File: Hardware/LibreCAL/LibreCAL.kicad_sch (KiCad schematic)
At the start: 4 parts

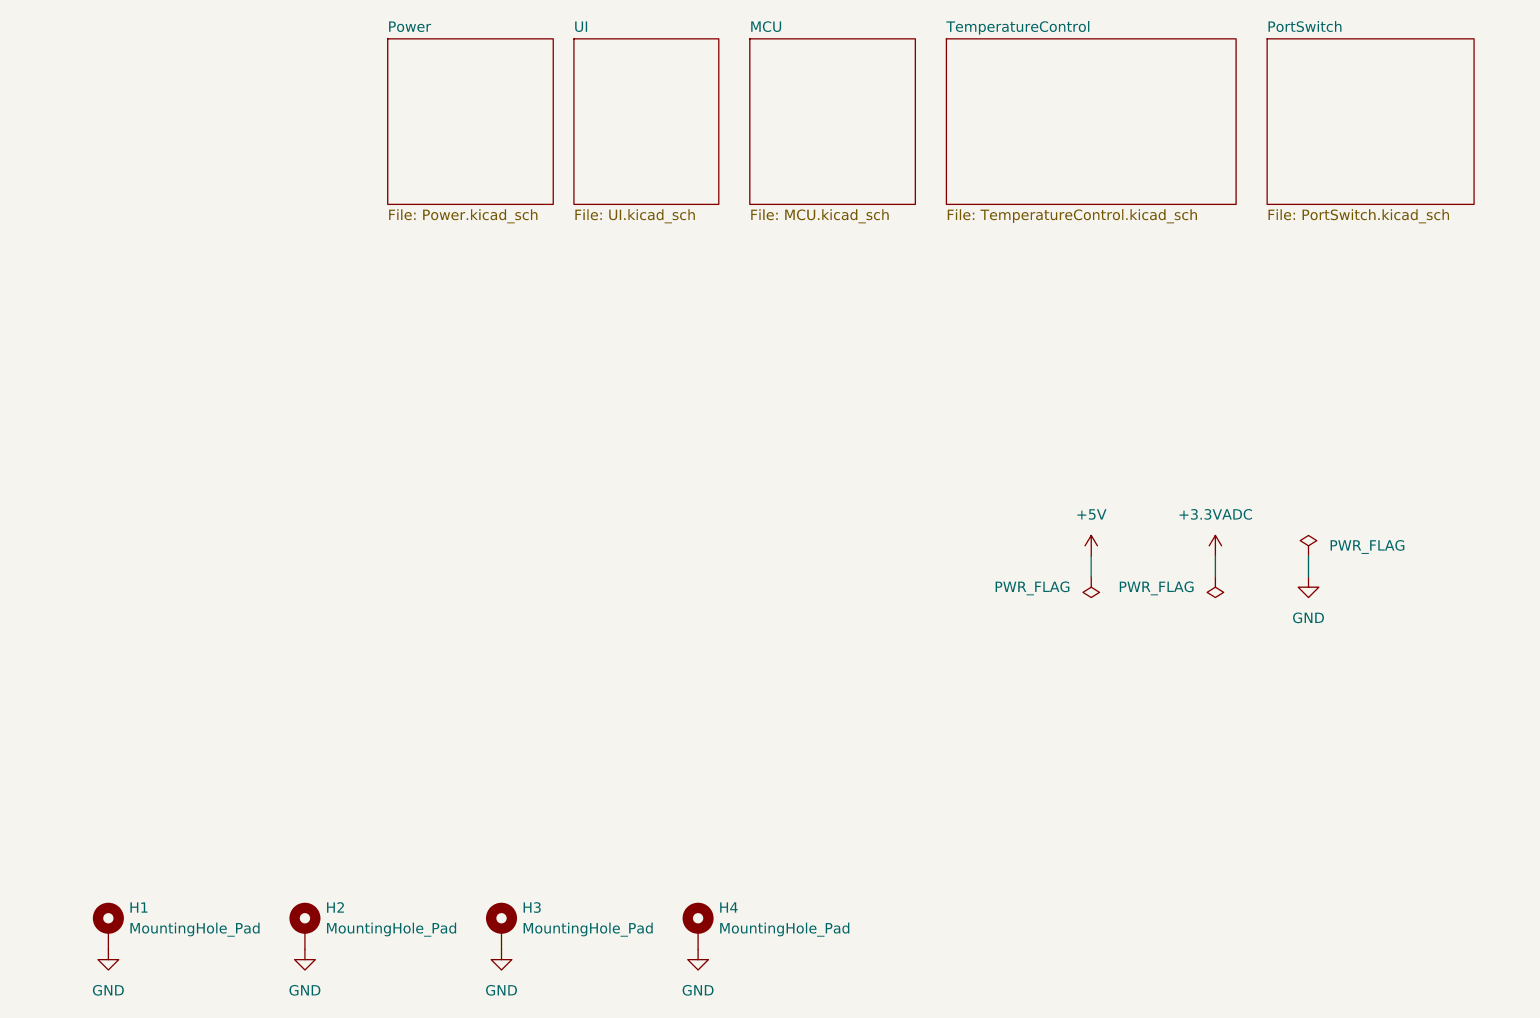
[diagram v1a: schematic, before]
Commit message: Filters added, housing updated
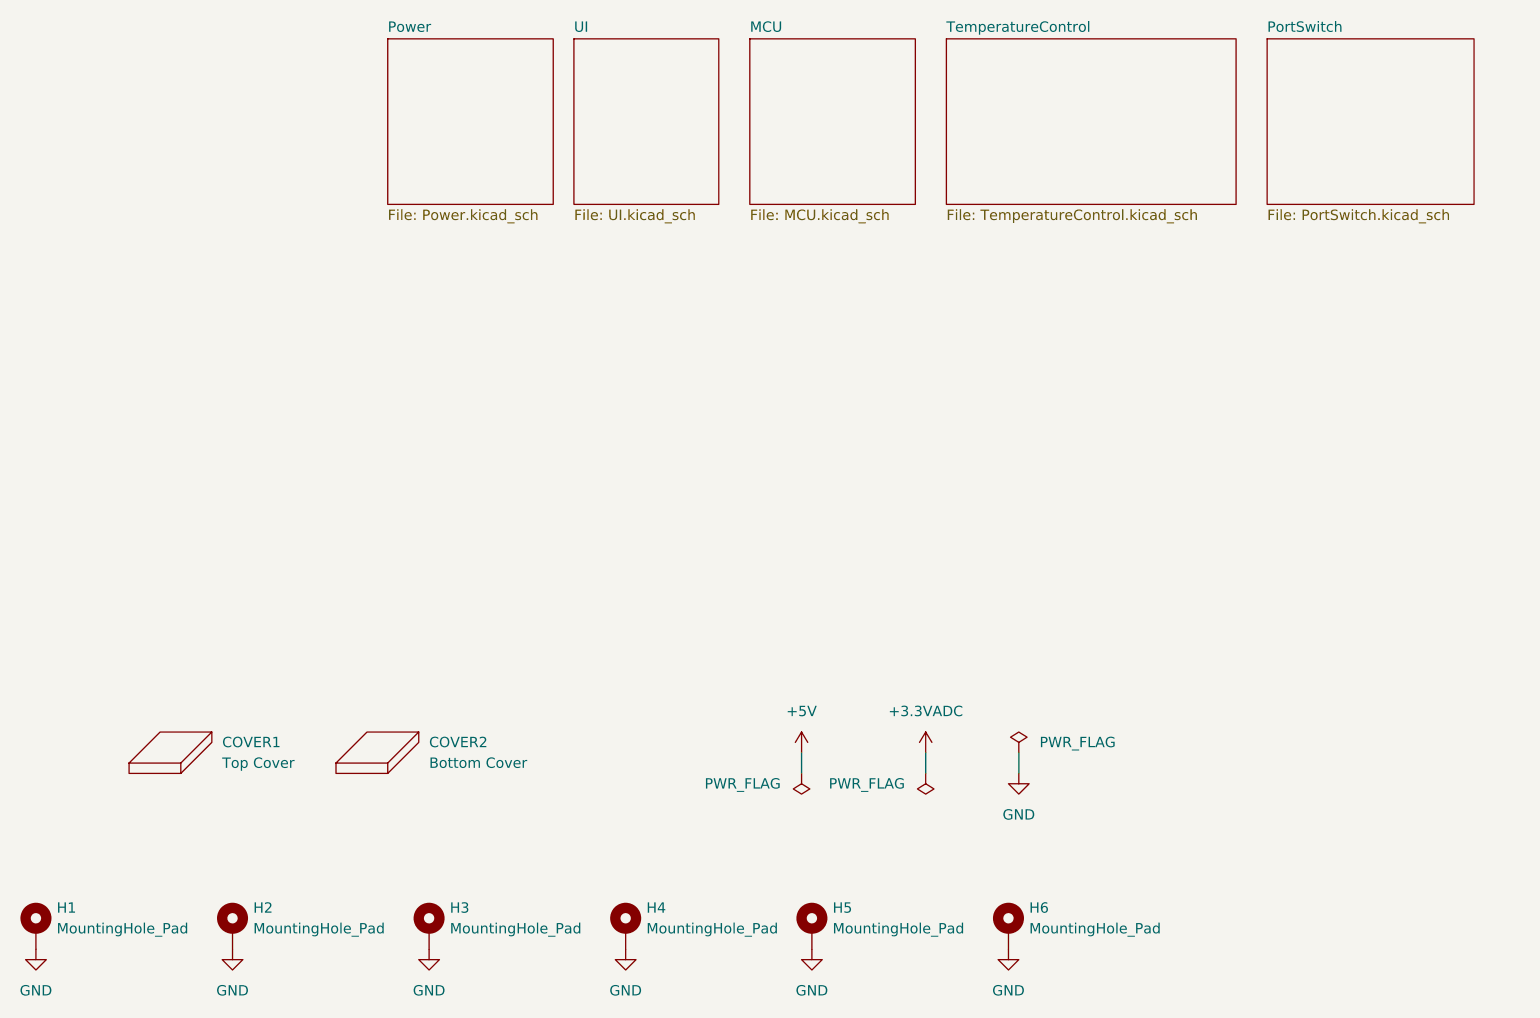
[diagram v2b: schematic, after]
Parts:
- added COVER1: Top Cover, LibreCAL:TopCover, symbol LibreCAL:Cover
- added COVER2: Bottom Cover, LibreCAL:BottomCover, symbol LibreCAL:Cover
- added H5, H6: MountingHole_Pad, MountingHole:MountingHole_3.2mm_M3_ISO14580_Pad_TopBottom, symbol Mechanical:MountingHole_Pad
- H1, H2, H3, H4: now left out of the parts list
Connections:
- net GND: now also H5.1, H6.1
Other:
- moved on the sheet: H1, H2, H3, H4

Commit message: Production files
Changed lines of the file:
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@@
     (pin "1")
+  )
+  (symbol (lib_id "LibreCAL:Cover") (at 72.39 154.94 0) (unit 1)
+    (in_bom no) (on_board yes) (fields_autoplaced)
+    (property "Reference" "COVER2" (id 0) (at 78.74 152.3999 0)
+      (effects (font (size 1.27 1.27)) (justify left))
+    )
+    (property "Value" "Bottom Cover" (id 1) (at 78.74 154.9399 0)
+      (effects (font (size 1.27 1.27)) (justify left))
+    )
+    (property "Footprint" "LibreCAL:BottomCover" (id 2) (at 72.39 154.94 0)
+      (effects (font (size 1.27 1.27)) hide)
+    )
+    (property "Datasheet" "" (id 3) (at 72.39 154.94 0)
+      (effects (font (size 1.27 1.27)) hide)
+    )
   )
   (symbol (lib_id "Mechanical:MountingHole_Pad") (at 149.86 176.53 0) (unit 1)
@@
     (pin "1")
   )
-  (symbol (lib_id "LibreCAL:Cover") (at 72.39 156.21 0) (unit 1)
+  (symbol (lib_id "LibreCAL:Cover") (at 46.99 154.94 0) (unit 1)
     (in_bom no) (on_board yes) (fields_autoplaced)
-    (property "Reference" "COVER2" (id 0) (at 78.74 153.6699 0)
-      (effects (font (size 1.27 1.27)) (justify left))
-    )
-    (property "Value" "Bottom Cover" (id 1) (at 78.74 156.2099 0)
-      (effects (font (size 1.27 1.27)) (justify left))
-    )
-    (property "Footprint" "LibreCAL:BottomCover" (id 2) (at 72.39 156.21 0)
-      (effects (font (size 1.27 1.27)) hide)
-    )
-    (property "Datasheet" "" (id 3) (at 72.39 156.21 0)
+    (property "Reference" "COVER1" (id 0) (at 53.34 152.3999 0)
+      (effects (font (size 1.27 1.27)) (justify left))
+    )
+    (property "Value" "Top Cover" (id 1) (at 53.34 154.9399 0)
+      (effects (font (size 1.27 1.27)) (justify left))
+    )
+    (property "Footprint" "LibreCAL:TopCover" (id 2) (at 46.99 154.94 0)
+      (effects (font (size 1.27 1.27)) hide)
+    )
+    (property "Datasheet" "" (id 3) (at 46.99 154.94 0)
       (effects (font (size 1.27 1.27)) hide)
     )
@@
     )
     (pin "1")
-  )
-  (symbol (lib_id "LibreCAL:Cover") (at 46.99 156.21 0) (unit 1)
-    (in_bom no) (on_board yes) (fields_autoplaced)
-    (property "Reference" "COVER1" (id 0) (at 53.34 153.6699 0)
-      (effects (font (size 1.27 1.27)) (justify left))
-    )
-    (property "Value" "Top Cover" (id 1) (at 53.34 156.2099 0)
-      (effects (font (size 1.27 1.27)) (justify left))
-    )
-    (property "Footprint" "LibreCAL:TopCover" (id 2) (at 46.99 156.21 0)
-      (effects (font (size 1.27 1.27)) hide)
-    )
-    (property "Datasheet" "" (id 3) (at 46.99 156.21 0)
-      (effects (font (size 1.27 1.27)) hide)
-    )
   )
   (symbol (lib_id "power:GND") (at 151.13 157.48 0) (unit 1)
@@
       (reference "C50") (unit 1) (value "NFM18CC223R1C3D") (footprint "LibreCAL:NFM18CC")
     )
-    (path "/dcda2e3f-39cb-4b5d-a0f7-3f67f2dd2c02"
+    (path "/a5774e18-31e1-4bb5-a8f4-b8516b668c1a"
       (reference "COVER1") (unit 1) (value "Top Cover") (footprint "LibreCAL:TopCover")
     )
-    (path "/ac162879-7480-449d-8f17-09ac1fe716ba"
+    (path "/3789b0ae-08e6-4dfa-af0f-48751ba38e44"
       (reference "COVER2") (unit 1) (value "Bottom Cover") (footprint "LibreCAL:BottomCover")
     )

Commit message: Improvements on LibreCAL KiCad: fixed minor errors/labels(cosmetic), improved BOM(Added LCSC_Part), improved Impedance JLCPCB 4Layer JLC7628 1.6mm
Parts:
- COVER1, COVER2, H1, H2, H3, H4, H5, H6: LCSC_Part (none) -> NA
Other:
- title: (none) -> LibreCAL
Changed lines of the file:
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@@
 (kicad_sch (version 20211123) (generator eeschema)
   (paper "A4")
+  (title_block
+    (title "LibreCAL")
+    (date "2023-01-07")
+    (rev "A+")
+  )
   (wire (pts (xy 124.46 154.94) (xy 124.46 157.48))
     (stroke (width 0) (type default) (color 0 0 0 0))
@@
       (effects (font (size 1.27 1.27)) hide)
     )
+    (property "LCSC_Part" "NA" (id 4) (at 72.39 154.94 0)
+      (effects (font (size 1.27 1.27)) hide)
+    )
   )
   (symbol (lib_id "Mechanical:MountingHole_Pad") (at 149.86 176.53 0) (unit 1)
@@
       (effects (font (size 1.27 1.27)) hide)
     )
+    (property "LCSC_Part" "NA" (id 4) (at 149.86 176.53 0)
+      (effects (font (size 1.27 1.27)) hide)
+    )
     (pin "1")
   )
@@
       (effects (font (size 1.27 1.27)) hide)
     )
+    (property "LCSC_Part" "NA" (id 4) (at 78.74 176.53 0)
+      (effects (font (size 1.27 1.27)) hide)
+    )
     (pin "1")
   )
@@
       (effects (font (size 1.27 1.27)) hide)
     )
+    (property "LCSC_Part" "NA" (id 4) (at 102.87 176.53 0)
+      (effects (font (size 1.27 1.27)) hide)
+    )
     (pin "1")
   )
@@
       (effects (font (size 1.27 1.27)) hide)
     )
+    (property "LCSC_Part" "NA" (id 4) (at 125.73 176.53 0)
+      (effects (font (size 1.27 1.27)) hide)
+    )
     (pin "1")
   )
@@
       (effects (font (size 1.27 1.27)) hide)
     )
+    (property "LCSC_Part" "NA" (id 4) (at 46.99 154.94 0)
+      (effects (font (size 1.27 1.27)) hide)
+    )
   )
   (symbol (lib_id "Mechanical:MountingHole_Pad") (at 54.61 176.53 0) (unit 1)
@@
       (effects (font (size 1.27 1.27)) hide)
     )
+    (property "LCSC_Part" "NA" (id 4) (at 54.61 176.53 0)
+      (effects (font (size 1.27 1.27)) hide)
+    )
     (pin "1")
   )
@@
     )
     (property "Datasheet" "~" (id 3) (at 30.48 176.53 0)
+      (effects (font (size 1.27 1.27)) hide)
+    )
+    (property "LCSC_Part" "NA" (id 4) (at 30.48 176.53 0)
       (effects (font (size 1.27 1.27)) hide)
     )
@@
       (reference "H6") (unit 1) (value "MountingHole_Pad") (footprint "MountingHole:MountingHole_3.2mm_M3_ISO14580_Pad_TopBottom")
     )
+    (path "/b660bab9-7028-47fa-8717-20664ec48a2d/eedd732f-bc34-40b5-93ce-5ec25d6b8d91"
+      (reference "J1") (unit 1) (value "901-10510-2") (footprint "LibreCAL:901-10510-2")
+    )
     (path "/b660bab9-7028-47fa-8717-20664ec48a2d/c4c4b9fd-653b-42a2-a6d7-d3104868ddd8"
-      (reference "J1") (unit 1) (value "901-10510-2") (footprint "LibreCAL:901-10510-2")
+      (reference "J2") (unit 1) (value "901-10510-2") (footprint "LibreCAL:901-10510-2")
+    )
+    (path "/b660bab9-7028-47fa-8717-20664ec48a2d/39a5cbeb-3a92-45be-a413-ca98d7475e60"
+      (reference "J3") (unit 1) (value "901-10510-2") (footprint "LibreCAL:901-10510-2")
     )
     (path "/b660bab9-7028-47fa-8717-20664ec48a2d/4b460ffd-1e31-4f25-8b61-70acf1f7a519"
-      (reference "J2") (unit 1) (value "901-10510-2") (footprint "LibreCAL:901-10510-2")
-    )
-    (path "/b660bab9-7028-47fa-8717-20664ec48a2d/eedd732f-bc34-40b5-93ce-5ec25d6b8d91"
-      (reference "J3") (unit 1) (value "901-10510-2") (footprint "LibreCAL:901-10510-2")
-    )
-    (path "/b660bab9-7028-47fa-8717-20664ec48a2d/39a5cbeb-3a92-45be-a413-ca98d7475e60"
       (reference "J4") (unit 1) (value "901-10510-2") (footprint "LibreCAL:901-10510-2")
     )
@@
     )
     (path "/b660bab9-7028-47fa-8717-20664ec48a2d/cd1b9f15-d921-4037-a512-0f5441bb33c5"
-      (reference "R1") (unit 1) (value "49R9") (footprint "Resistor_SMD:R_0402_1005Metric")
+      (reference "R1") (unit 1) (value "CH0402-50RGFTA") (footprint "Resistor_SMD:R_0402_1005Metric")
     )
     (path "/b660bab9-7028-47fa-8717-20664ec48a2d/cc17f03b-4abd-4310-bf7c-9776f9183981"
-      (reference "R2") (unit 1) (value "49R9") (footprint "Resistor_SMD:R_0402_1005Metric")
+      (reference "R2") (unit 1) (value "CH0402-50RGFTA") (footprint "Resistor_SMD:R_0402_1005Metric")
     )
     (path "/b660bab9-7028-47fa-8717-20664ec48a2d/0ac4026e-cd83-430f-8205-8259072b6065"
-      (reference "R3") (unit 1) (value "49R9") (footprint "Resistor_SMD:R_0402_1005Metric")
+      (reference "R3") (unit 1) (value "CH0402-50RGFTA") (footprint "Resistor_SMD:R_0402_1005Metric")
     )
     (path "/b660bab9-7028-47fa-8717-20664ec48a2d/841e6434-1104-4dd6-b0d3-9344d1358c68"
-      (reference "R4") (unit 1) (value "49R9") (footprint "Resistor_SMD:R_0402_1005Metric")
+      (reference "R4") (unit 1) (value "CH0402-50RGFTA") (footprint "Resistor_SMD:R_0402_1005Metric")
     )
     (path "/8ae04189-9a62-4c2c-b6af-68aaa5063c12/b1924762-6311-472e-a458-ad91d9625da7"
